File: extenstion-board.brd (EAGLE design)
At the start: 91.4 x 73.3 mm, 13 parts

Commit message: added provision screw plug
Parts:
- removed X1, X10, X11, X12, X13, X2, X3, X4, X5, X6, X7, X8, X9: (no value), con-wago-500:W237-102
- added J1, J10, J11, J12, J13, J2, J3, J4, J5, J6, J7, J8, J9: (no value), SparkFun-Connectors:1X02_XTRA_BIG
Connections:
- net +12V: now also J1.1, J10.2, J2.2, J4.1, J5.2, J7.1, J8.2; no longer X1.2, X13.1, X2.1, X4.2, X5.1, X7.2, X8.1
- net GND: now also J1.2, J10.1, J3.1, J4.2, J6.1, J7.2, J9.1; no longer X1.1, X13.2, X3.2, X4.1, X6.2, X7.1, X9.2
- net N$1: now also J11.2, J8.1; no longer X12.1, X8.2
- net N$2: now also J13.2, J2.1; no longer X10.1, X2.2
- net N$3: now also J13.1, J3.2; no longer X10.2, X3.1
- net N$4: now also J12.2, J5.1; no longer X11.1, X5.2
- net N$5: now also J12.1, J6.2; no longer X11.2, X6.1
- net N$6: now also J11.1, J9.2; no longer X12.2, X9.1
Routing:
- net +12V: track 181.0 -> 163.0 mm
- net N$6: track 58.8 -> 53.0 mm
- net N$1: track 50.1 -> 48.8 mm
- net N$4: track 41.7 -> 40.4 mm
- net N$3: track 43.8 -> 42.5 mm
- net N$5: track 45.9 -> 44.6 mm
- net N$2: track 48.0 -> 46.7 mm

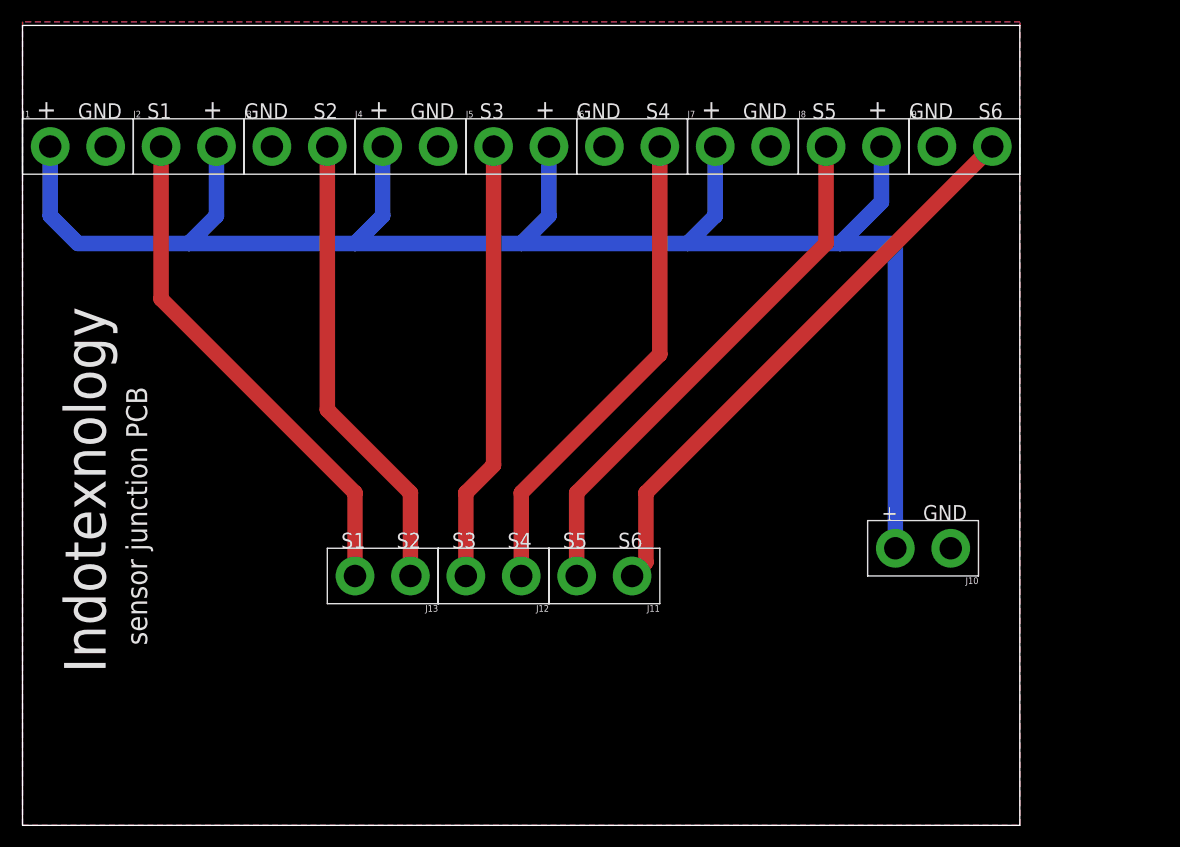
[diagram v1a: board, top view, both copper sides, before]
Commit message: added holes for pillers
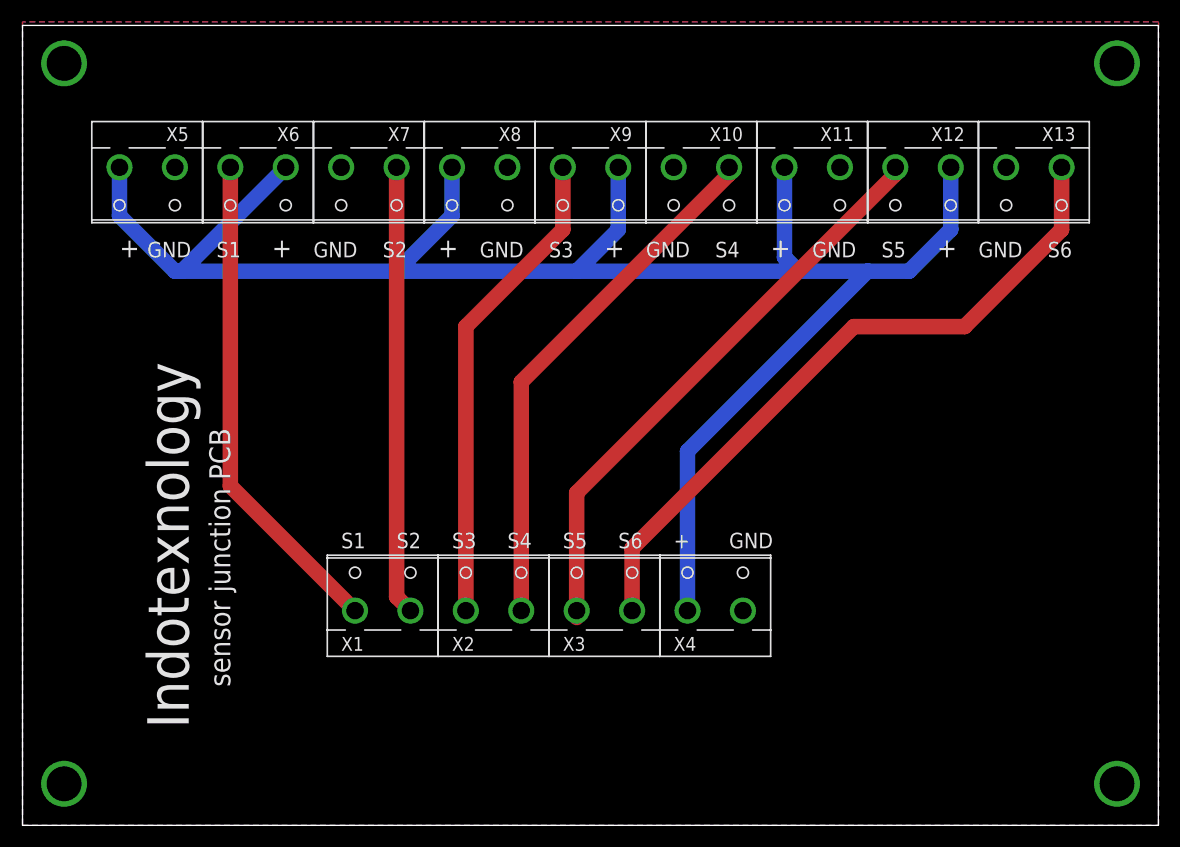
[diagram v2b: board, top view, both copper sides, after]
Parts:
- removed J1, J10, J11, J12, J13, J2, J3, J4, J5, J6, J7, J8, J9: (no value), SparkFun-Connectors:1X02_XTRA_BIG
- added X1, X10, X11, X12, X13, X2, X3, X4, X5, X6, X7, X8, X9: (no value), pluggable-con:W237-132
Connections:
- net +12V: now also X11.2, X12.1, X4.1, X5.2, X6.1, X8.2, X9.1; no longer J1.1, J10.2, J2.2, J4.1, J5.2, J7.1, J8.2
- net GND: now also X10.2, X11.1, X13.2, X4.2, X5.1, X7.2, X8.1; no longer J1.2, J10.1, J3.1, J4.2, J6.1, J7.2, J9.1
- net N$1: now also X12.2, X3.1; no longer J11.2, J8.1
- net N$2: now also X1.1, X6.2; no longer J13.2, J2.1
- net N$3: now also X1.2, X7.1; no longer J13.1, J3.2
- net N$4: now also X2.1, X9.2; no longer J12.2, J5.1
- net N$5: now also X10.1, X2.2; no longer J12.1, J6.2
- net N$6: now also X13.1, X3.2; no longer J11.1, J9.2
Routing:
- net +12V: track 163.0 -> 174.2 mm
- net N$6: track 53.0 -> 62.9 mm
- net N$1: track 48.8 -> 53.4 mm
- net N$4: track 40.4 -> 44.3 mm
- net N$5: track 44.6 -> 48.5 mm
- net N$3: track 42.5 -> 41.2 mm
- net N$2: track 46.7 -> 45.4 mm
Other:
- board size 91.4 x 73.3 mm -> 104.1 x 73.3 mm
